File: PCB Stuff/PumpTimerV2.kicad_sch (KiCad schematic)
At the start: 33 parts, among them J2 282856-2, J3 282856-2, J4 Conn_02x20_Odd_Even, J6 B4B-PH-SM4-TBT(LF)(SN), K1 ADW1205HLW, K2 ADW1205HLW, Q1 DMN67D7L, Q2 DMN67D7L, SW1 TL3305AF160QG, U1 RX8900UA

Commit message: Added temp sensor. Started adding to PCB but not yet placed or routed.
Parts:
- removed J6: B4B-PH-SM4-TBT(LF)(SN), Connector_JST:JST_PH_B4B-PH-SM4-TB_1x04-1MP_P2.00mm_Vertical, symbol Connector_Generic:Conn_01x04
- added R6, R7: 2k2, Resistor_SMD:R_0603_1608Metric_Pad0.98x0.95mm_HandSolder, symbol Device:R_US
- added U2: TCN75AVOA, Package_SO:SOIC-8_3.9x4.9mm_P1.27mm, symbol TZ_Sensors:TCN75AVOA
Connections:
- net +3V3: now also R6.1, R7.1
- net GND: now also U2.4 (GND), U2.5 (A2), U2.6 (A1)
- net GPIO2(SDA1): now also U2.1 (SDA)
- net GPIO3(SCL1): now also U2.2 (SCL)
- net ~{TEMP_ALERT}: now reaches J4.16 (Pin_16)
- net ~{TEMP_ALERT}: now also R6.2, U2.3 (ALERT)
- net RTC_~{INT} renamed ~{RTC_INT}
- new net: R7.2, U2.7 (A0)
- new net +3.3V: U2.8 (VDD)
- no-connect marks 27 -> 26
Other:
- note added: "I2C Temp Sensor"
- note added: "Temp sensor address 0x01"
- note removed: "I2C Expansion Port (just in case)"
- note removed: "SWAP THIS FOR A THERMAL SENSOR OF SOME KIND"

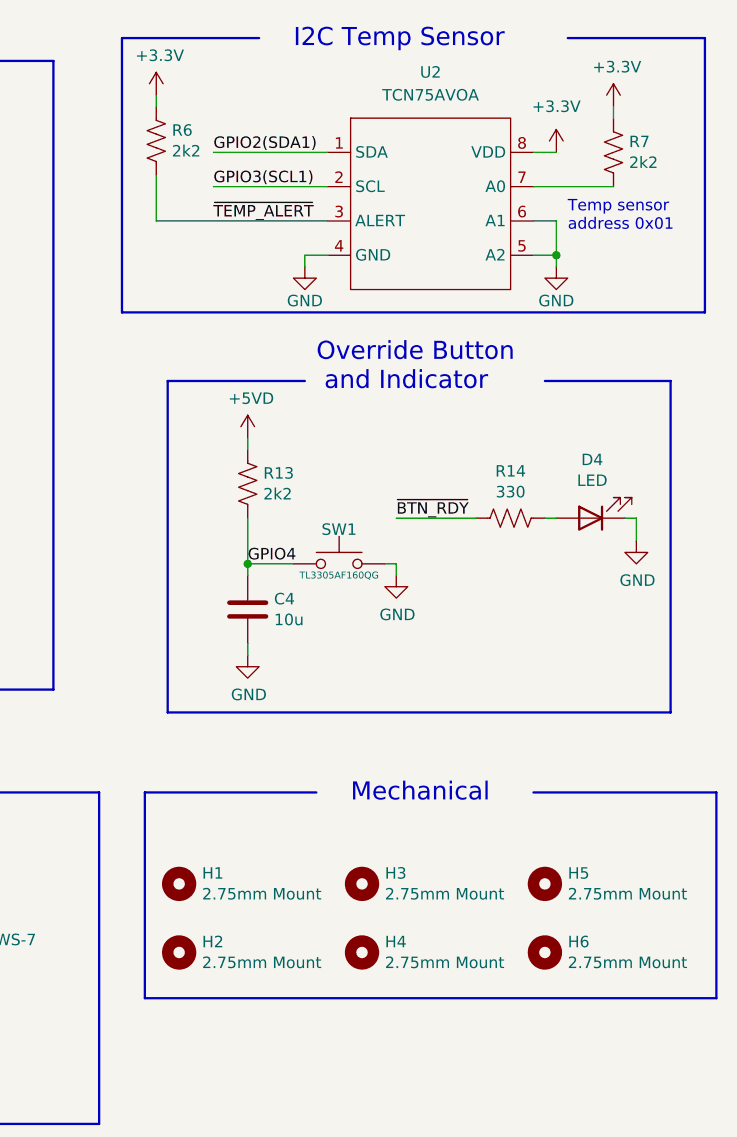
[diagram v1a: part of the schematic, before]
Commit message: Rerouted PCB with temp sensor in place
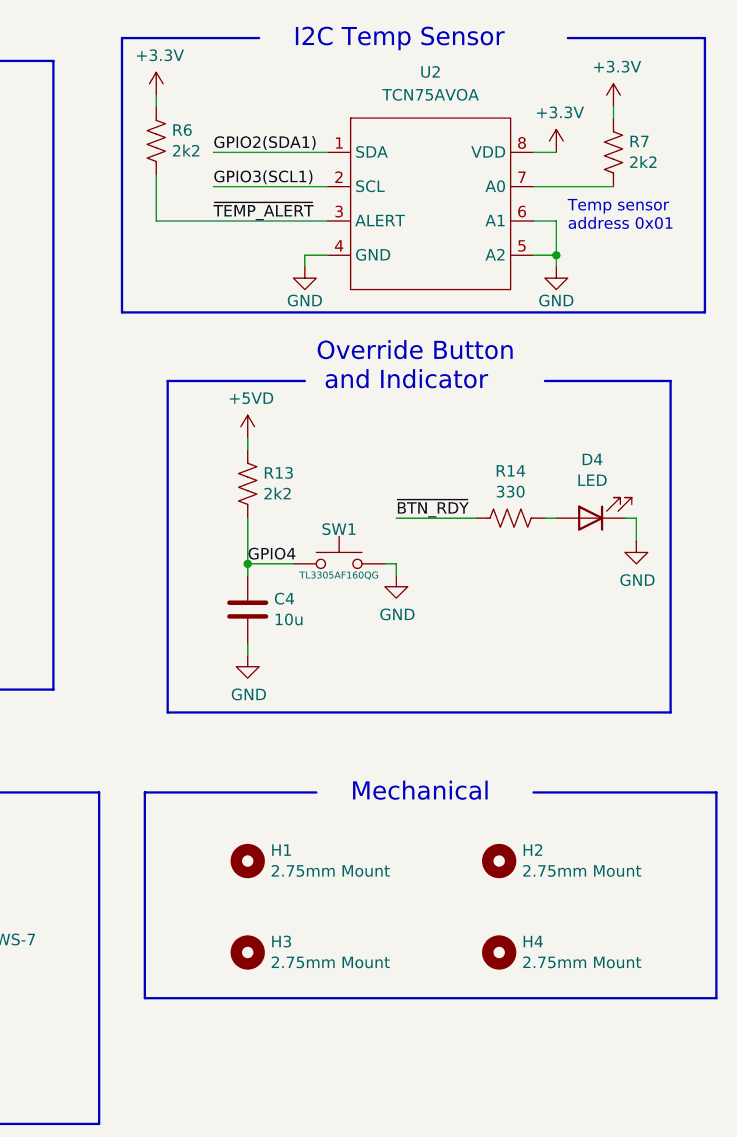
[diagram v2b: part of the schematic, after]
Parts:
- removed H2, H5: 2.75mm Mount, MountingHole:MountingHole_2.7mm_M2.5, symbol Mechanical:MountingHole
- renumbered H3 to H2, H4 to H3, H6 to H4
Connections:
- net +3.3V is gone; now on net +3V3: U2.8 (VDD)
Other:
- moved on the sheet: H1, H2, H3, H4

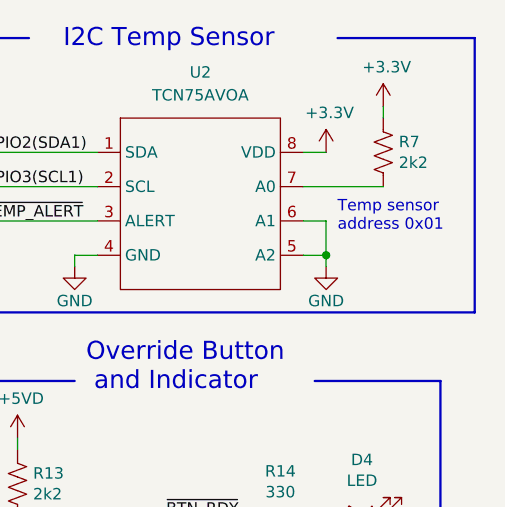
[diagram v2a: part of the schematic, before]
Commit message: Added temp sensor operations
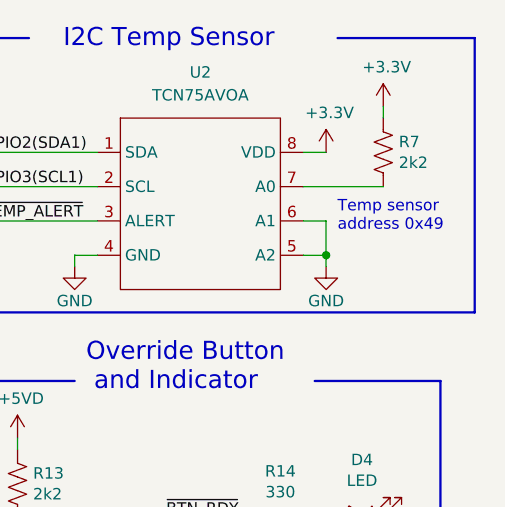
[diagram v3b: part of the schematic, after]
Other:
- note added: "Temp sensor address 0x49"
- note removed: "Temp sensor address 0x01"
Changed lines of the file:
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@@
     (effects (font (size 2.0066 2.0066)) (justify left bottom))
   )
-  (text "Temp sensor\naddress 0x01" (at 266.7 49.53 0)
+  (text "Temp sensor\naddress 0x49" (at 266.7 49.53 0)
     (effects (font (size 1.27 1.27)) (justify left bottom))
   )
